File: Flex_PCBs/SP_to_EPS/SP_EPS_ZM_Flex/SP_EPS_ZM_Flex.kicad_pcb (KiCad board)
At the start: 2 copper layers, 4.5 x 60 mm, 2 parts, among them J1 Conn_01x08_Male, J2 Conn_01x08_Male

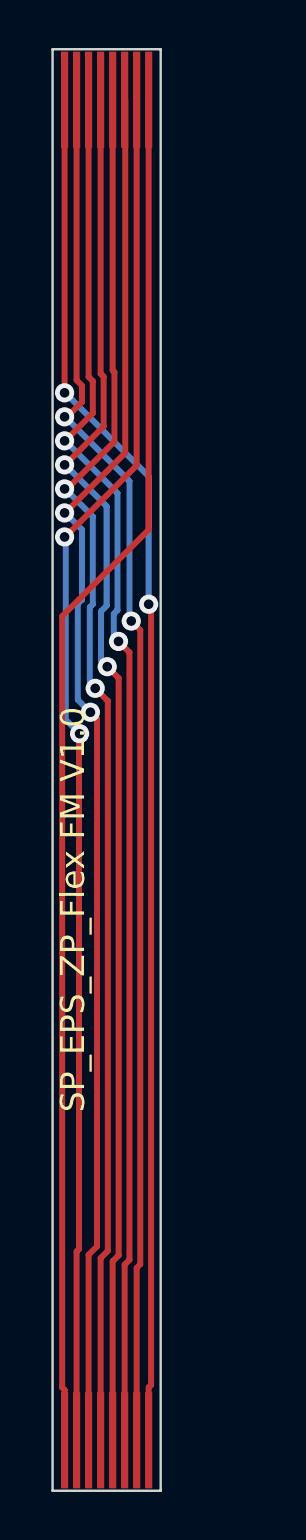
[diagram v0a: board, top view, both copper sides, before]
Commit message: replace ZF5S-*-01-T-WT and 2005280040 connectors with T1M-*-F-SH-L-FR connector
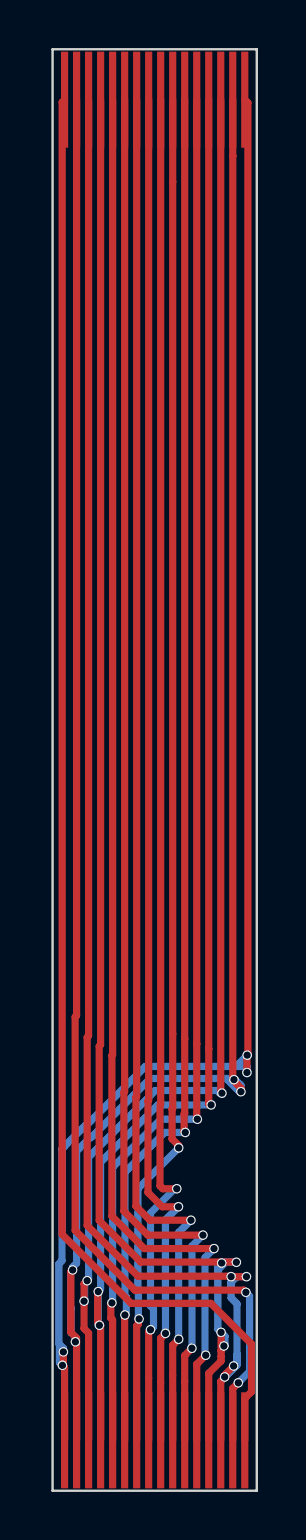
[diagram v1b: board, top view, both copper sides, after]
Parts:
- J1, J2: value Conn_01x08_Male -> Conn_01x16_Pin; footprint STS_connector:flexpcb con. -> STS_connector:flexpcb_con_z_minus
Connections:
- J1 pad 1: 8 -> 1
- J1 pad 2: 7 -> 2
- J1 pad 3: 6 -> 3
- J1 pad 4: 5 -> 4
- J1 pad 5: 4 -> 5
- J1 pad 6: 3 -> 6
- J1 pad 7: 2 -> 7
- J1 pad 8: 1 -> 8
- J2 pad 1: 1 -> 16
- J2 pad 2: 2 -> 15
- J2 pad 3: 3 -> 14
- J2 pad 4: 4 -> 13
- J2 pad 5: 5 -> 12
- J2 pad 6: 6 -> 11
- J2 pad 7: 7 -> 10
- J2 pad 8: 8 -> 9
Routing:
- net 15: track 0.00 -> 66.4 mm, vias 0 -> 4
- net 16: track 0.00 -> 64.3 mm, vias 0 -> 4
- net 14: track 0.00 -> 61.0 mm, vias 0 -> 3
- net 13: track 0.00 -> 60.7 mm, vias 0 -> 3
- net 12: track 0.00 -> 58.2 mm, vias 0 -> 2
- net 11: track 0.00 -> 57.4 mm, vias 0 -> 2
- net 9: track 0.00 -> 57.1 mm, vias 0 -> 2
- net 10: track 0.00 -> 56.7 mm, vias 0 -> 2
- net 3: track 57.7 -> 63.6 mm, vias 2 -> 4
- net 4: track 57.7 -> 62.4 mm, vias 2 -> 4
- net 2: track 57.4 -> 61.8 mm
- net 1: track 57.3 -> 61.2 mm
- net 5: track 57.8 -> 59.6 mm
- net 6: track 57.7 -> 58.8 mm
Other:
- board size 4.5 x 60 mm -> 8.5 x 60 mm
- board text removed: "SP_EPS_ZP_Flex FM V1.0"
